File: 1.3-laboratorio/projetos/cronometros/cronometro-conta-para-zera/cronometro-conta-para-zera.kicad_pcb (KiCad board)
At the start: 2 copper layers, 65 parts, among them J1 Barrel_Jack_Switch, SW1 SW_Push, SW2 SW_Push, U1 LM555, U10 CD4511BNSR, U11 HDSP-7803, U12 HDSP-7803, U13 HDSP-7803, U14 HDSP-7803, U2 74HC4518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

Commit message: Posicionamento dos componentes na PCI.
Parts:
- moved C15 50.8 mm to (207.6, 27.9), turned to 180 degrees
- moved R4 43.4 mm to (214.0, 88.0)
- moved C4 43.1 mm to (157.5, 93.0)
- moved C8 43.0 mm to (223.2, 27.9), turned to 180 degrees
- moved C3 42.9 mm to (208.9, 93.0)
- moved U6 42.8 mm to (202.6, 33.0), turned to 0 degrees
- moved U5 41.6 mm to (187.0, 33.0), turned to 0 degrees
- moved R5 41.6 mm to (152.4, 88.0)
- moved C7 39.4 mm to (238.8, 27.9), turned to 180 degrees
- moved U3 34.7 mm to (218.1, 31.8), turned to 0 degrees
- moved C10 34.2 mm to (176.5, 27.9), turned to 180 degrees
- moved SW2 30.7 mm to (188.0, 102.2)
- moved U2 30.6 mm to (233.7, 31.8), turned to 0 degrees
- moved SW1 30.5 mm to (171.4, 102.2)
- moved U11 30.1 mm to (193.0, 85.7)
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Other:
- board outline added: 118.1 x 88.9 mm

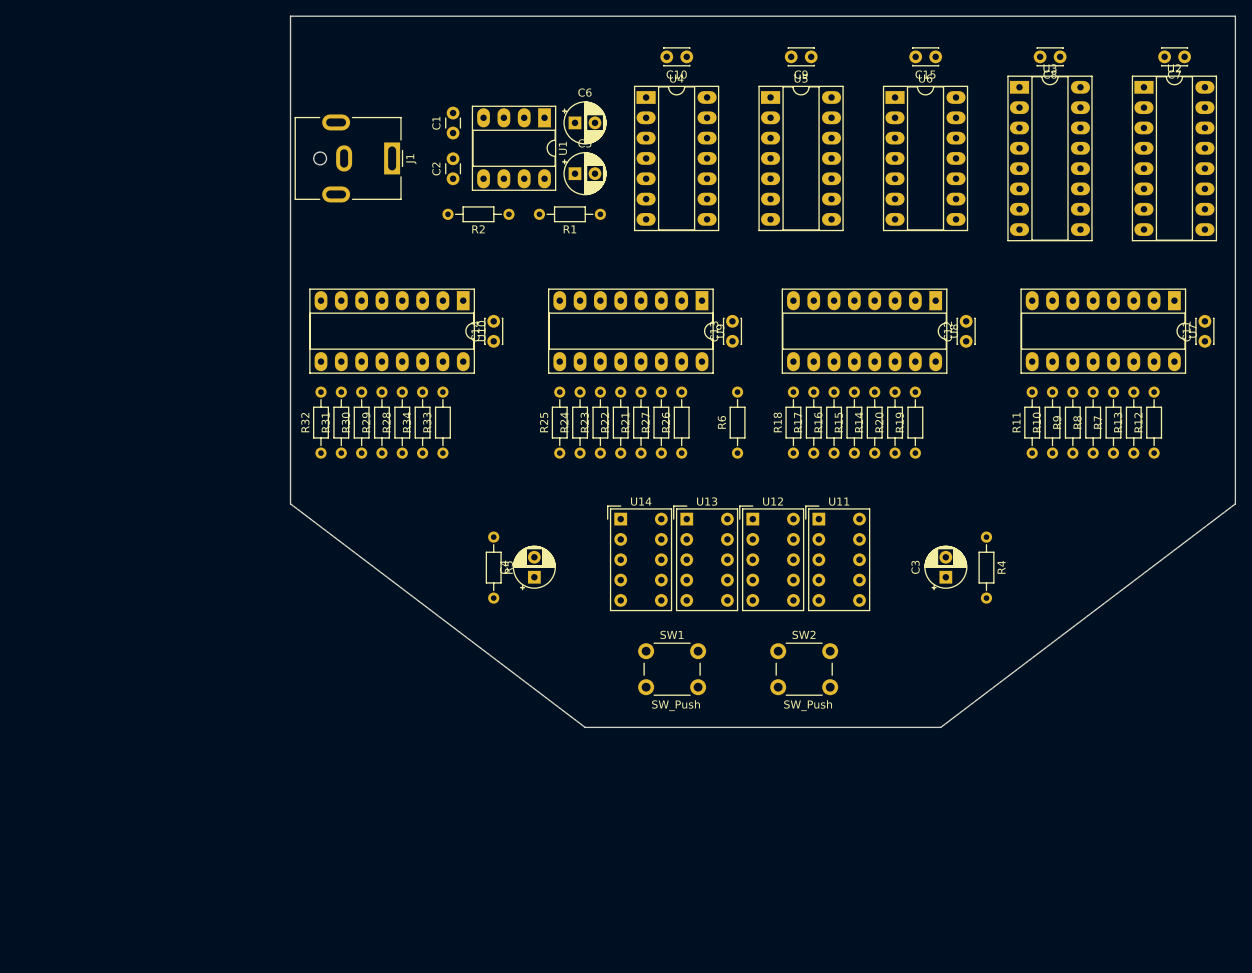
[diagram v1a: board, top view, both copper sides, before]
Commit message: Roteamento e contorno da placa.
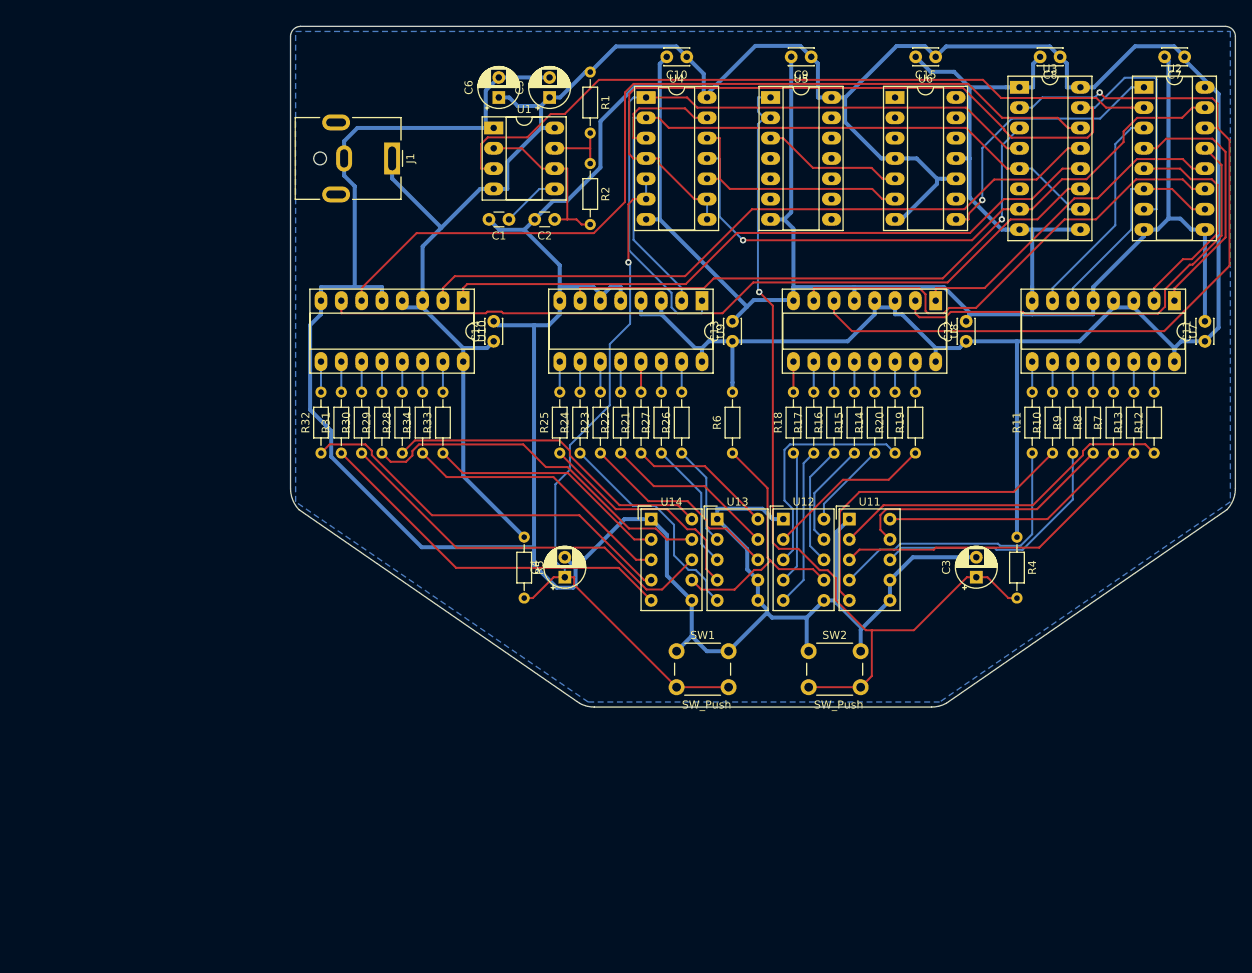
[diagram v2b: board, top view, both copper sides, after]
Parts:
- moved R1 17.8 mm to (164.5, 29.8), turned to 270 degrees
- moved C2 13.7 mm to (160.0, 48.3), turned to 180 degrees
- moved C1 12.9 mm to (154.3, 48.3), turned to 180 degrees
- moved R2 12.0 mm to (164.5, 41.3), turned to 270 degrees
- moved C5 10.0 mm to (159.4, 33.0), turned to 90 degrees
- moved C6 10.0 mm to (153.0, 33.0), turned to 90 degrees
- moved U1 6.48 mm to (152.4, 36.8), turned to 0 degrees
- moved C3 3.81 mm to (212.7, 93.0)
- moved C4 3.81 mm to (161.3, 93.0)
- moved R4 3.81 mm to (217.8, 88.0)
- moved R5 3.81 mm to (156.2, 88.0)
- moved SW1 3.81 mm to (175.3, 102.2)
- moved SW2 3.81 mm to (191.8, 102.2)
- moved U11 3.81 mm to (196.8, 85.7)
- moved U12 3.81 mm to (188.6, 85.7)
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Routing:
- net Earth: track 0.00 -> 576.7 mm
- net VCC: track 0.00 -> 391.1 mm
- net MR: track 0.00 -> 117.3 mm
- net Net-(C3-Pad1): track 0.00 -> 114.1 mm, vias 0 -> 1
- net /M3: track 0.00 -> 112.3 mm
- net /Su3: track 0.00 -> 103.9 mm, vias 0 -> 1
- net /M0: track 0.00 -> 100.6 mm
- net ck: track 0.00 -> 92.3 mm
- net Net-(C4-Pad1): track 0.00 -> 89.2 mm, vias 0 -> 1
- net /M2: track 0.00 -> 88.5 mm
- net /Sd2: track 0.00 -> 86.3 mm
- net /Sd1: track 0.00 -> 85.2 mm
- net /M1: track 0.00 -> 84.9 mm
- net /clr_seg: track 0.00 -> 78.4 mm, vias 0 -> 1
- net /Sd0: track 0.00 -> 70.2 mm, vias 0 -> 1
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- added copper zone on B.Cu, net Earth
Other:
- board size 118.1 x 88.9 mm -> 118.1 x 85.1 mm

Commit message: Leiaute praticamente final do cronômetro. Faltam últimas revisões.
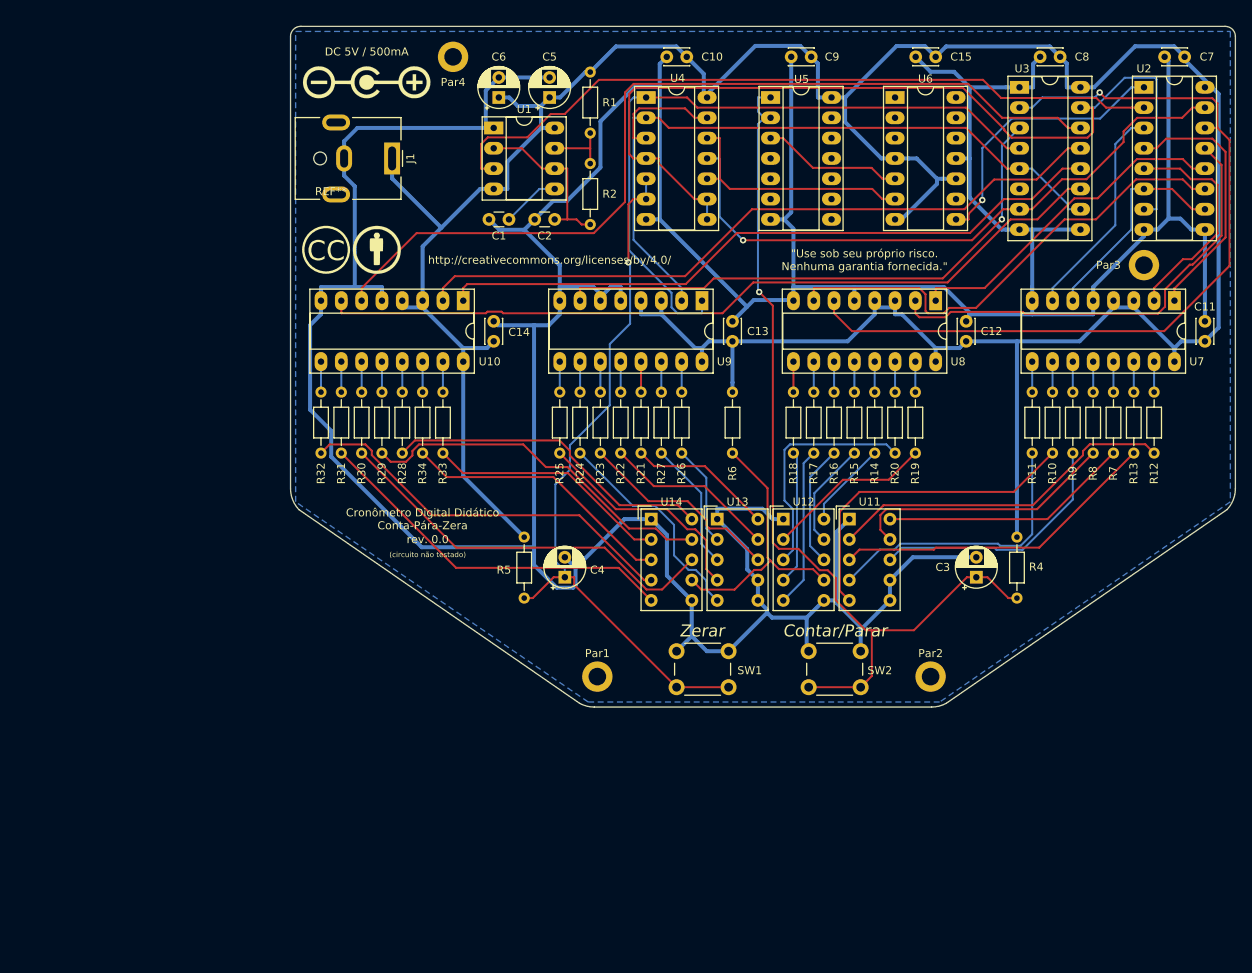
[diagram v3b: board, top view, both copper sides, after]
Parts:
- added G***: LOGO, contornos-personalizados:Symbol_CreativeCommonsBY_6mm_SilkScreenTop, F.Cu at (137.8, 52.1)
- added G***: LOGO, contornos-personalizados:Polarity_Center_Positive_4mm_SilkScreen, F.Cu at (136.5, 31.1)
- added Par1: MountingHole_2.2mm_M2_DIN965_Pad, MountingHole:MountingHole_2.2mm_M2_DIN965_Pad, F.Cu at (165.4, 105.4)
- added Par2: MountingHole_2.2mm_M2_DIN965_Pad, MountingHole:MountingHole_2.2mm_M2_DIN965_Pad, F.Cu at (207.0, 105.4)
- added Par3: MountingHole_2.2mm_M2_DIN965_Pad, MountingHole:MountingHole_2.2mm_M2_DIN965_Pad, F.Cu at (233.7, 54.0)
- added Par4: MountingHole_2.2mm_M2_DIN965_Pad, MountingHole:MountingHole_2.2mm_M2_DIN965_Pad, F.Cu at (147.3, 27.9)
- added REF**: Symbol_CreativeCommons_SilkScreenTop_Type2_Small, contornos-personalizados:Symbol_CreativeCommons_SilkScreenTop_Type2_Small, F.Cu at (131.4, 52.1)
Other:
- board text added: ""Use sob seu próprio risco. Nenhuma garantia fornecida.""
- board text added: "(circuito não testado)"
- board text added: "Contar/Parar"
- board text added: "Cronômetro Digital Didático Conta-Pára-Zera"
- board text added: "DC 5V / 500mA"
- board text added: "Zerar"
- board text added: "http://creativecommons.org/licenses/by/4.0/"
- board text added: "rev. 0.0"

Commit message: Projeto concluído do Cronômetro Digital Didático Conta-Pára-Zera.
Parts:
- moved Par1 46.3 mm to (131.1, 136.5)
- moved R4 46.3 mm to (183.5, 119.1)
- moved U14 46.3 mm to (137.8, 116.8)
- moved Par3 46.3 mm to (199.4, 85.1)
- moved U2 46.3 mm to (199.4, 62.9)
- moved U3 46.3 mm to (183.8, 62.9)
- moved C11 46.3 mm to (207.0, 94.6)
- moved C12 46.3 mm to (177.2, 94.6)
- moved C15 46.3 mm to (173.4, 59.1)
- moved R11 46.3 mm to (185.4, 108.6)
- moved R15 46.3 mm to (163.2, 108.6)
- moved R18 46.3 mm to (155.6, 108.6)
- moved R23 46.3 mm to (131.4, 108.6)
- moved R26 46.3 mm to (141.6, 108.6)
- moved R5 46.3 mm to (121.9, 119.1)
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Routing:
- net Earth: track 576.7 -> 0.00 mm
